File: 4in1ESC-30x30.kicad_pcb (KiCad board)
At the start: 6 copper layers, 41.6 x 42.5 mm, 226 parts, among them J1 SM08B-SRSS-TB, Q1 C22385416, Q10 C22385416, Q11 C22385416, Q12 C22385416, Q13 C22385416, Q14 C22385416, Q15 C22385416, Q16 C22385416, Q17 C22385416, Q18 C22385416, Q19 C22385416, Q2 C22385416, Q20 C22385416, Q21 C22385416, Q22 C22385416, Q23 C22385416, Q24 C22385416, Q3 C22385416, Q4 C22385416, Q5 C22385416, Q6 C22385416, Q7 C22385416, Q8 C22385416, Q9 C22385416, U1 TLV76733DRVR, U10 AT32F421G8U7, U11 NSG2065Q, U12 INA186A3IDCKR, U18 LMR51420YDDCR, U2 AT32F421G8U7, U4 NSG2065Q, U5 XRIM160808SR47MBCD, U6 AT32F421G8U7, U7 NSG2065Q, U8 AT32F421G8U7, U9 NSG2065Q

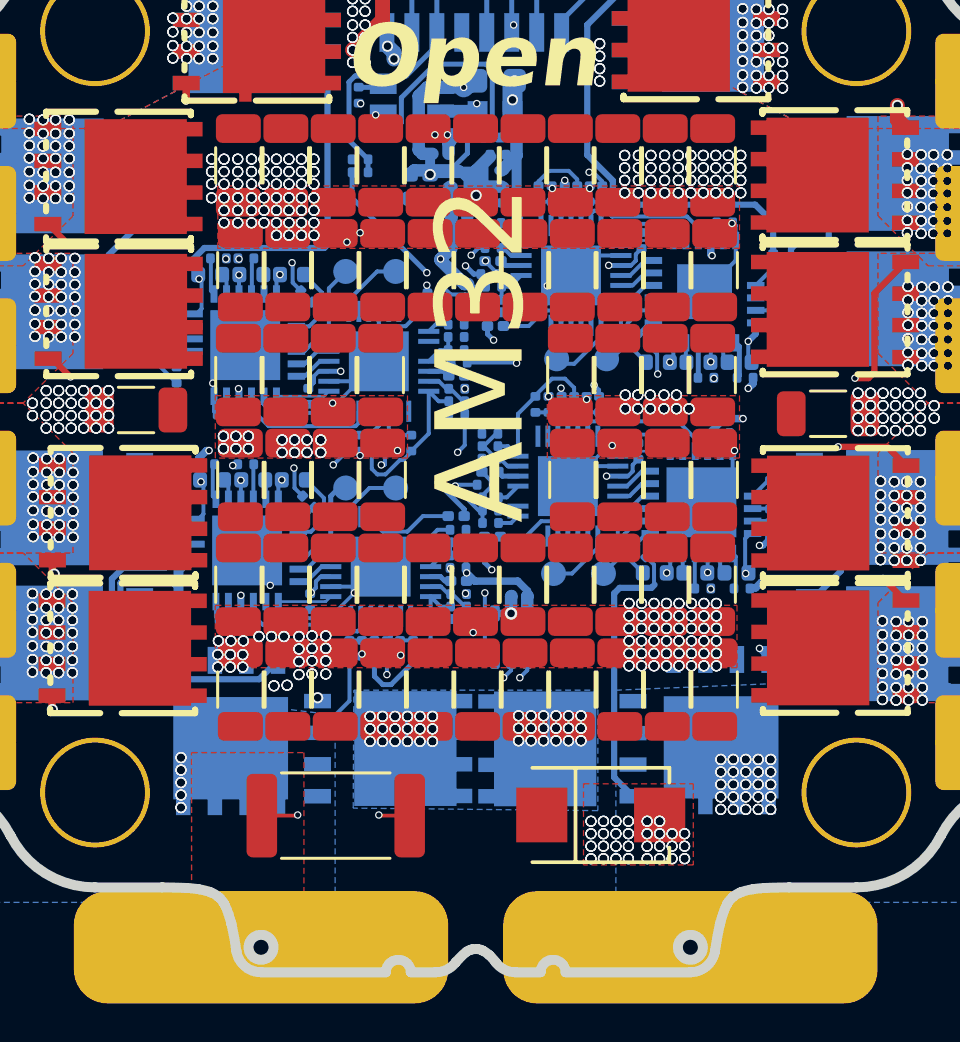
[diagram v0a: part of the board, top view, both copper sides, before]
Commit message: Final parts changes and production files for V0.1
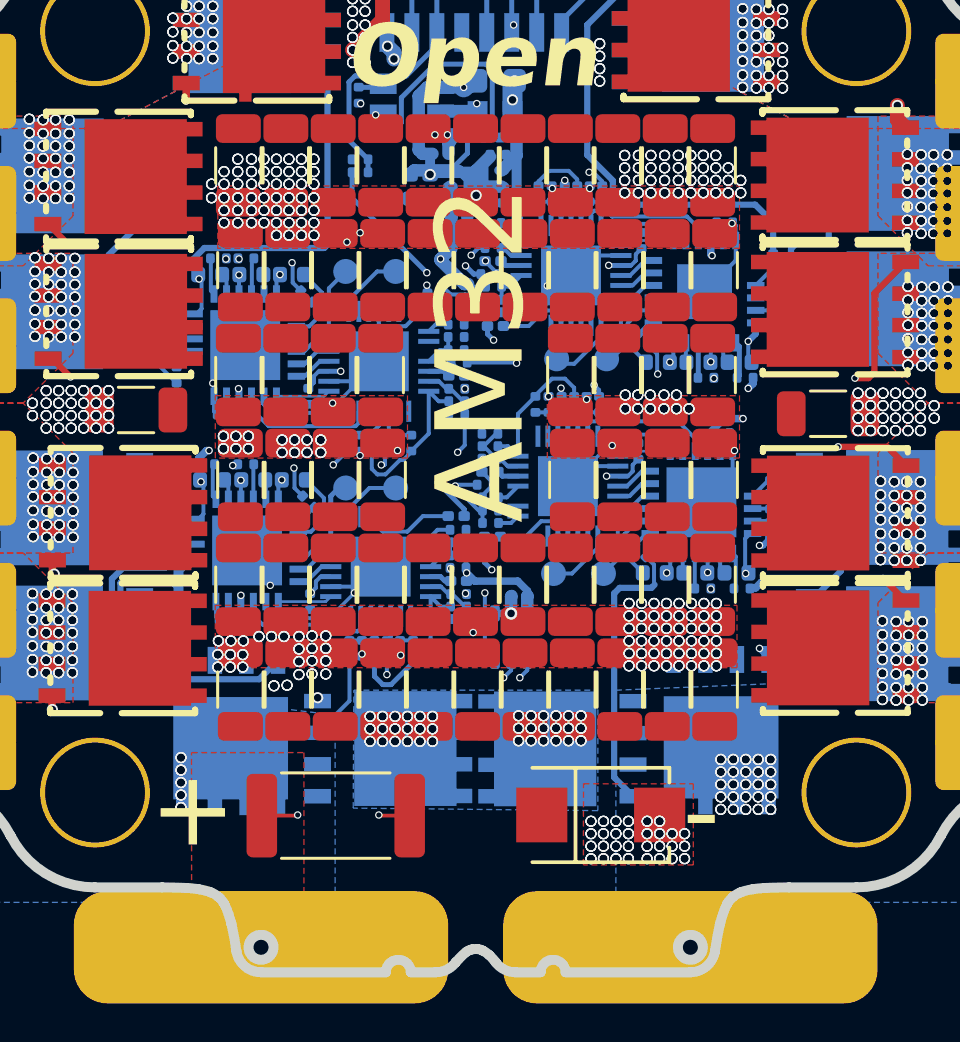
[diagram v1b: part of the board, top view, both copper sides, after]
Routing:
- net GND: vias 622 -> 610
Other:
- board text added: "+"
- board text added: "-"
- board text added: "3-6S INPUT"
- board text added: "4 3 2 1 T C - +"
